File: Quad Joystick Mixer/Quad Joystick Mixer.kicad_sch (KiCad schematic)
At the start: 5 parts

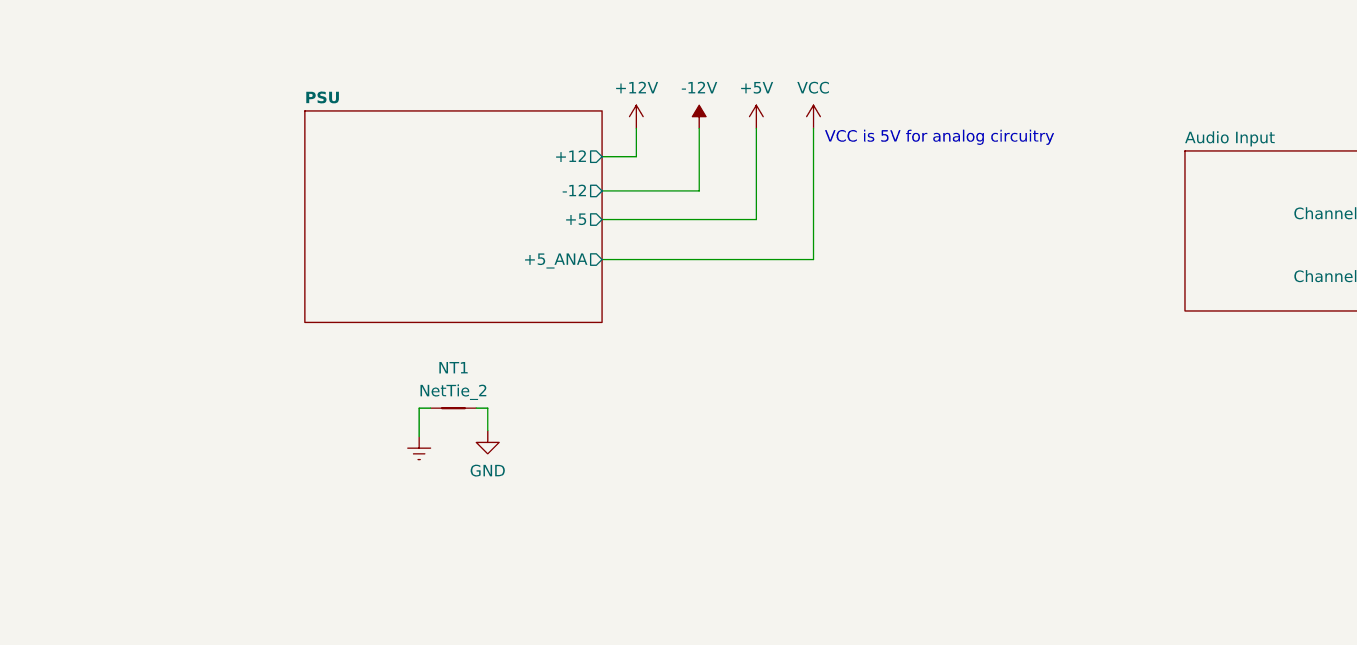
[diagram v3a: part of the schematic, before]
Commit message: finish adding parts to the BOM
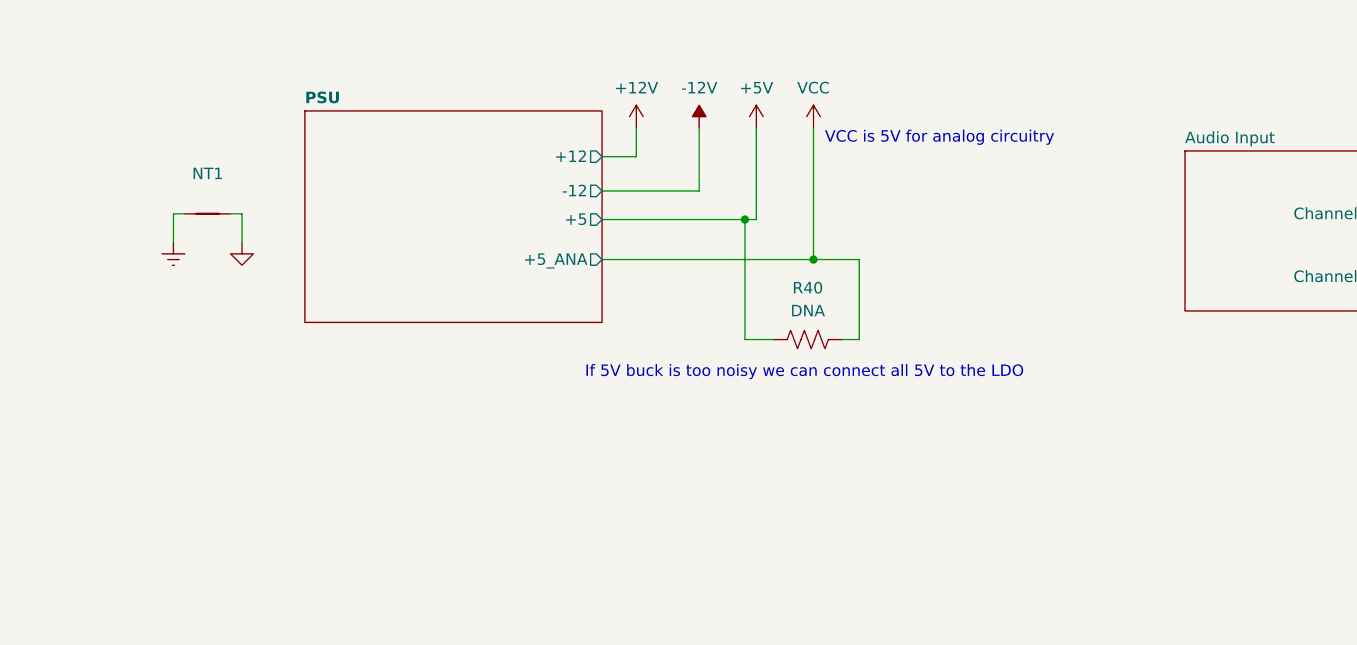
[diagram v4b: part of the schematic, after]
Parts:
- added R40: DNA, Resistor_SMD:R_2010_5025Metric_Pad1.40x2.65mm_HandSolder, symbol Device:R_US
- NT1: Source (none) -> NA
- R85, R86, R87, R88: footprint (none) -> Resistor_SMD:R_0805_2012Metric_Pad1.20x1.40mm_HandSolder; DK PN (none) -> NA; MPN (none) -> NA; Source (none) -> NA
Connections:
- net +5V: now also R40.1
- net VCC: now also R40.2
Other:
- note added: "If 5V buck is too noisy we can connect all 5V to the LDO"
- moved on the sheet: NT1
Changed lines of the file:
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@@
   (junction (at 276.86 71.755) (diameter 0) (color 0 0 0 0)
   )
+  (junction (at 186.69 49.53) (diameter 0) (color 0 0 0 0)
+  )
+  (junction (at 194.31 53.975) (diameter 0) (color 0 0 0 0)
+  )
   (junction (at 325.755 42.545) (diameter 0) (color 0 0 0 0)
   )
@@
     (stroke (width 0) (type default))
   )
+  (wire (pts (xy 186.69 62.865) (xy 186.69 49.53))
+    (stroke (width 0) (type default))
+  )
   (wire (pts (xy 297.18 29.21) (xy 277.495 29.21))
     (stroke (width 0) (type default))
   )
+  (wire (pts (xy 189.865 62.865) (xy 186.69 62.865))
+    (stroke (width 0) (type default))
+  )
   (wire (pts (xy 297.18 136.525) (xy 305.435 136.525))
     (stroke (width 0) (type default))
@@
     (stroke (width 0) (type default))
   )
+  (wire (pts (xy 199.39 62.865) (xy 199.39 53.975))
+    (stroke (width 0) (type default))
+  )
   (wire (pts (xy 337.82 149.86) (xy 342.265 149.86))
     (stroke (width 0) (type default))
   )
-  (wire (pts (xy 150.495 70.485) (xy 150.495 73.66))
+  (wire (pts (xy 123.19 48.895) (xy 123.19 52.07))
     (stroke (width 0) (type default))
   )
@@
     (stroke (width 0) (type default))
   )
-  (wire (pts (xy 158.115 73.025) (xy 158.115 70.485))
+  (wire (pts (xy 130.81 52.07) (xy 130.81 48.895))
     (stroke (width 0) (type default))
   )
@@
     (stroke (width 0) (type default))
   )
+  (wire (pts (xy 197.485 62.865) (xy 199.39 62.865))
+    (stroke (width 0) (type default))
+  )
   (wire (pts (xy 194.31 53.975) (xy 194.31 39.37))
     (stroke (width 0) (type default))
   )
-  (wire (pts (xy 170.815 49.53) (xy 187.96 49.53))
+  (wire (pts (xy 170.815 49.53) (xy 186.69 49.53))
+    (stroke (width 0) (type default))
+  )
+  (wire (pts (xy 186.69 49.53) (xy 187.96 49.53))
+    (stroke (width 0) (type default))
+  )
+  (wire (pts (xy 199.39 53.975) (xy 194.31 53.975))
     (stroke (width 0) (type default))
   )
@@
     (stroke (width 0) (type default))
   )
-  (wire (pts (xy 151.765 70.485) (xy 150.495 70.485))
+  (wire (pts (xy 124.46 48.895) (xy 123.19 48.895))
     (stroke (width 0) (type default))
   )
@@
     (stroke (width 0) (type default))
   )
-  (wire (pts (xy 158.115 70.485) (xy 156.845 70.485))
+  (wire (pts (xy 130.81 48.895) (xy 129.54 48.895))
     (stroke (width 0) (type default))
   )
@@
     (effects (font (size 1.27 1.27)) (justify left bottom))
   )
+  (text "If 5V buck is too noisy we can connect all 5V to the LDO"
+    (at 168.91 67.31 0)
+    (effects (font (size 1.27 1.27)) (justify left bottom))
+  )
   (text "VCC is 5V for analog circuitry" (at 195.58 41.275 0)
     (effects (font (size 1.27 1.27)) (justify left bottom))
@@
     (effects (font (size 1.27 1.27)) (justify left bottom))
   )
-  (symbol (lib_id "power:GND") (at 158.115 73.025 0) (unit 1)
+  (symbol (lib_id "power:GND") (at 130.81 52.07 0) (unit 1)
     (in_bom yes) (on_board yes) (dnp no) (fields_autoplaced)
-    (property "Reference" "#PWR094" (at 158.115 79.375 0)
-      (effects (font (size 1.27 1.27)) hide)
-    )
-    (property "Value" "GND" (at 158.115 77.47 0)
-      (effects (font (size 1.27 1.27)))
-    )
-    (property "Footprint" "" (at 158.115 73.025 0)
-      (effects (font (size 1.27 1.27)) hide)
-    )
-    (property "Datasheet" "" (at 158.115 73.025 0)
+    (property "Reference" "#PWR094" (at 130.81 58.42 0)
+      (effects (font (size 1.27 1.27)) hide)
+    )
+    (property "Value" "GND" (at 130.81 56.515 0)
+      (effects (font (size 1.27 1.27)) hide)
+    )
+    (property "Footprint" "" (at 130.81 52.07 0)
+      (effects (font (size 1.27 1.27)) hide)
+    )
+    (property "Datasheet" "" (at 130.81 52.07 0)
       (effects (font (size 1.27 1.27)) hide)
     )
@@
     )
   )
-  (symbol (lib_id "power:Earth") (at 150.495 73.66 0) (unit 1)
+  (symbol (lib_id "power:Earth") (at 123.19 52.07 0) (unit 1)
     (in_bom yes) (on_board yes) (dnp no) (fields_autoplaced)
-    (property "Reference" "#PWR095" (at 150.495 80.01 0)
-      (effects (font (size 1.27 1.27)) hide)
-    )
-    (property "Value" "Earth" (at 150.495 77.47 0)
-      (effects (font (size 1.27 1.27)) hide)
-    )
-    (property "Footprint" "" (at 150.495 73.66 0)
-      (effects (font (size 1.27 1.27)) hide)
-    )
-    (property "Datasheet" "~" (at 150.495 73.66 0)
+    (property "Reference" "#PWR095" (at 123.19 58.42 0)
+      (effects (font (size 1.27 1.27)) hide)
+    )
+    (property "Value" "Earth" (at 123.19 55.88 0)
+      (effects (font (size 1.27 1.27)) hide)
+    )
+    (property "Footprint" "" (at 123.19 52.07 0)
+      (effects (font (size 1.27 1.27)) hide)
+    )
+    (property "Datasheet" "~" (at 123.19 52.07 0)
       (effects (font (size 1.27 1.27)) hide)
     )
@@
       (effects (font (size 1.27 1.27)))
     )
-    (property "Footprint" "" (at 302.514 70.739 90)
+    (property "Footprint" "Resistor_SMD:R_0805_2012Metric_Pad1.20x1.40mm_HandSolder" (at 302.514 70.739 90)
       (effects (font (size 1.27 1.27)) hide)
     )
     (property "Datasheet" "~" (at 302.26 71.755 0)
+      (effects (font (size 1.27 1.27)) hide)
+    )
+    (property "Source" "NA" (at 302.26 71.755 0)
+      (effects (font (size 1.27 1.27)) hide)
+    )
+    (property "DK PN" "NA" (at 302.26 71.755 0)
+      (effects (font (size 1.27 1.27)) hide)
+    )
+    (property "MPN" "NA" (at 302.26 71.755 0)
       (effects (font (size 1.27 1.27)) hide)
     )
@@
       (effects (font (size 1.27 1.27)))
     )
-    (property "Footprint" "" (at 301.879 65.659 90)
+    (property "Footprint" "Resistor_SMD:R_0805_2012Metric_Pad1.20x1.40mm_HandSolder" (at 301.879 65.659 90)
       (effects (font (size 1.27 1.27)) hide)
     )
     (property "Datasheet" "~" (at 301.625 66.675 0)
+      (effects (font (size 1.27 1.27)) hide)
+    )
+    (property "Source" "NA" (at 301.625 66.675 0)
+      (effects (font (size 1.27 1.27)) hide)
+    )
+    (property "DK PN" "NA" (at 301.625 66.675 0)
+      (effects (font (size 1.27 1.27)) hide)
+    )
+    (property "MPN" "NA" (at 301.625 66.675 0)
       (effects (font (size 1.27 1.27)) hide)
     )
@@
     )
   )
-  (symbol (lib_id "Device:NetTie_2") (at 154.305 70.485 0) (unit 1)
+  (symbol (lib_id "Device:NetTie_2") (at 127 48.895 0) (unit 1)
     (in_bom no) (on_board yes) (dnp no) (fields_autoplaced)
-    (property "Reference" "NT1" (at 154.305 66.04 0)
+    (property "Reference" "NT1" (at 127 44.45 0)
       (effects (font (size 1.27 1.27)))
     )
-    (property "Value" "NetTie_2" (at 154.305 68.58 0)
-      (effects (font (size 1.27 1.27)))
-    )
-    (property "Footprint" "NetTie:NetTie-2_SMD_Pad2.0mm" (at 154.305 70.485 0)
-      (effects (font (size 1.27 1.27)) hide)
-    )
-    (property "Datasheet" "~" (at 154.305 70.485 0)
+    (property "Value" "NetTie_2" (at 127 46.99 0)
+      (effects (font (size 1.27 1.27)) hide)
+    )
+    (property "Footprint" "NetTie:NetTie-2_SMD_Pad2.0mm" (at 127 48.895 0)
+      (effects (font (size 1.27 1.27)) hide)
+    )
+    (property "Datasheet" "~" (at 127 48.895 0)
+      (effects (font (size 1.27 1.27)) hide)
+    )
+    (property "Source" "NA" (at 127 48.895 0)
       (effects (font (size 1.27 1.27)) hide)
     )
@@
       (effects (font (size 1.27 1.27)))
     )
-    (property "Footprint" "" (at 301.244 22.479 90)
+    (property "Footprint" "Resistor_SMD:R_0805_2012Metric_Pad1.20x1.40mm_HandSolder" (at 301.244 22.479 90)
       (effects (font (size 1.27 1.27)) hide)
     )
     (property "Datasheet" "~" (at 300.99 23.495 0)
+      (effects (font (size 1.27 1.27)) hide)
+    )
+    (property "Source" "NA" (at 300.99 23.495 0)
+      (effects (font (size 1.27 1.27)) hide)
+    )
+    (property "DK PN" "NA" (at 300.99 23.495 0)
+      (effects (font (size 1.27 1.27)) hide)
+    )
+    (property "MPN" "NA" (at 300.99 23.495 0)
       (effects (font (size 1.27 1.27)) hide)
     )
@@
       (effects (font (size 1.27 1.27)))
     )
-    (property "Footprint" "" (at 301.244 28.194 90)
+    (property "Footprint" "Resistor_SMD:R_0805_2012Metric_Pad1.20x1.40mm_HandSolder" (at 301.244 28.194 90)
       (effects (font (size 1.27 1.27)) hide)
     )
     (property "Datasheet" "~" (at 300.99 29.21 0)
+      (effects (font (size 1.27 1.27)) hide)
+    )
+    (property "Source" "NA" (at 300.99 29.21 0)
+      (effects (font (size 1.27 1.27)) hide)
+    )
+    (property "DK PN" "NA" (at 300.99 29.21 0)
+      (effects (font (size 1.27 1.27)) hide)
+    )
+    (property "MPN" "NA" (at 300.99 29.21 0)
       (effects (font (size 1.27 1.27)) hide)
     )
@@
         )
       )
+    )
+  )
+  (symbol (lib_id "Device:R_US") (at 193.675 62.865 90) (unit 1)
+    (in_bom yes) (on_board yes) (dnp no) (fields_autoplaced)
+    (property "Reference" "R40" (at 193.675 57.15 90)
+      (effects (font (size 1.27 1.27)))
+    )
+    (property "Value" "DNA" (at 193.675 59.69 90)
+      (effects (font (size 1.27 1.27)))
+    )
+    (property "Footprint" "Resistor_SMD:R_2010_5025Metric_Pad1.40x2.65mm_HandSolder" (at 193.929 61.849 90)
+      (effects (font (size 1.27 1.27)) hide)
+    )
+    (property "Datasheet" "~" (at 193.675 62.865 0)
+      (effects (font (size 1.27 1.27)) hide)
+    )
+    (pin "1")
+    (pin "2")
+    (instances
+      (project "Quad Joystick Mixer"
+        (path "/e9da4955-68c1-4335-ab8e-8a9cc0328d2d/547597e7-7fd4-4461-bc12-6ec4a58ef011"
+          (reference "R40") (unit 1)
+        )
+        (path "/e9da4955-68c1-4335-ab8e-8a9cc0328d2d"
+          (reference "R40") (unit 1)
+        )
+      )

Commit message: changed power supply design and everything re routed
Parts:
- R40: Source (none) -> NA
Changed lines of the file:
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@@
+      (effects (font (size 1.27 1.27)) hide)
+    )
+    (property "Source" "NA" (at 193.675 62.865 0)
       (effects (font (size 1.27 1.27)) hide)
     )
